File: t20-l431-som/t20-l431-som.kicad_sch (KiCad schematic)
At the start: 2 parts, among them U1 STM32L431-WLCSP64, U2 T20W80

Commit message: Continued initial work on t20-l431 som
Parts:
- removed unit 2 of U2
- removed unit 5 of U2
- removed unit 4 of U2
- U1: footprint (none) -> azonenberg_pcb:BGA_64_0.35MM_3p1MM_STM32L431
- U2: footprint (none) -> azonenberg_pcb:BGA_80_0.4MM_4p4x3p5_T20W80
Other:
- added sheet FPGA config (fpga-config.kicad_sch)
- added sheet Unused banks (unused.kicad_sch)
- sheet Power ports: added 1V8, 3V3, GND, VBAT; removed none
- note added: "Required boot mode straps for SPI x1 mode: * TEST_N high * SS_N high * CBUS[2:0] = 3'b111 We want to avoid needing five external resistors Can we reuse these signals for MCU - FPGA traffic where possible?"
- note added: "TODO: host connection"
- moved on the sheet: U1A, U1B, U1C, U1D, U1E, U2C, U2F, U2G

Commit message: Continued initial layout
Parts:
- added U4: MODULE_INTERNAL_T20_L431_HOST, azonenberg_pcb:MODULE_INTERNAL_T20_L431_HOST, symbol special-azonenberg:MODULE_INTERNAL_T20_L431_HOST
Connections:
- net GPIOL_74_PLLIN0: now reaches U2.A2 (GPIOL_74_PLLIN0)
- net GPIOL_74_PLLIN0: now also U4.B1 (GPIOL_74_PLLIN0)
- net GPIOL_72: now reaches U2.B2 (GPIOL_72_EXTFB0_CDI14)
- net GPIOL_72: now also U4.B2 (GPIOL_72_EXTFB0_CDI14)
- net GPIOL_69_CBSEL1: now reaches U2.C1 (GPIOL_69_CBSEL1)
- net GPIOL_69_CBSEL1: now also U4.B4 (GPIOL_69_CBSEL1)
- net GPIOL_70_CBSEL0: now reaches U2.D1 (GPIOL_70_CBSEL0)
- net GPIOL_70_CBSEL0: now also U4.A4 (GPIOL_70_CBSEL0)
- net GPIOL_71_NSTATUS: now reaches U2.E1 (GPIOL_71_NSTATUS)
- net GPIOL_71_NSTATUS: now also U4.B5 (GPIOL_71_NSTATUS)
- net GPIOL_46: now reaches U2.E2 (GPIOL_46)
- net GPIOL_46: now also U4.C5 (GPIOL_46)
- net GPIOL_25_CLK1: now reaches U2.F1 (GPIOL_25_CLK1)
- net GPIOL_25_CLK1: now also U4.A5 (GPIOL_25_CLK1)
- net GPIOL_24_CLK0: now reaches U2.G1 (GPIOL_24_CLK0)
- net GPIOL_24_CLK0: now also U4.A6 (GPIOL_24_CLK0)
- net GPIOL_20_CTRL0_CDI4: now reaches U2.G2 (GPIOL_20_CTRL0_CDI4)
- net GPIOL_20_CTRL0_CDI4: now also U4.B6 (GPIOL_20_CTRL0_CDI4)
- net GPIOL_13_CDI3: now reaches U2.H1 (GPIOL_13_CDI3)
- net GPIOL_13_CDI3: now also U4.A8 (GPIOL_13_CDI3)
- net GPIOL_12_CDI2: now reaches U2.H2 (GPIOL_12_CDI2)
- net GPIOL_12_CDI2: now also U4.A7 (GPIOL_12_CDI2)
- net GPIOR_133_CDI18: now reaches U2.H7 (GPIOR_133_CDI18)
- net GPIOR_133_CDI18: now also U4.F7 (GPIOR_133_CDI18)
- net CROSS_SPI_MOSI: now reaches U2.H8 (GPIOR_149_CBUS2)
- net CROSS_SPI_MOSI: now also U1.F2 (PB15)
- net GPIOR_154: now reaches U2.J6 (GPIOR_154)
- net GPIOR_154: now also U4.E8 (GPIOR_154)
- net CROSS_SPI_CS_N: now reaches U2.J7 (GPIOR_151_CBUS0)
- net CROSS_SPI_CS_N: now also U1.G3 (PB12)
- net CROSS_SPI_SCK: now reaches U2.J8 (GPIOR_150_CBUS1)
- net CROSS_SPI_SCK: now also U1.G2 (PB13)
- net GPIOR_155: now reaches U2.K6 (GPIOR_155)
- net GPIOR_155: now also U4.E9 (GPIOR_155)
- net CROSS_SPI_MISO: now reaches U2.K7 (GPIOR_158_TEST_N)
- net CROSS_SPI_MISO: now also U1.G1 (PB14)
- net GPIOR_76_PLLIN0: now reaches U2.E7 (GPIOR_76_PLLIN0)
- net GPIOR_76_PLLIN0: now also U4.E5 (GPIOR_76_PLLIN0)
- net GPIOR_116_CTRL15: now reaches U2.G7 (GPIOR_116_CTRL15)
- net GPIOR_116_CTRL15: now also U4.E6 (GPIOR_116_CTRL15)
- net GPIOR_117_CTRL14: now reaches U2.H5 (GPIOR_117_CTRL14)
- net GPIOR_117_CTRL14: now also U4.E7 (GPIOR_117_CTRL14)
- net GPIOR_122_CLK13_CDI21: now reaches U2.H6 (GPIOR_122_CLK13_CDI21)
- net GPIOR_122_CLK13_CDI21: now also U4.F6 (GPIOR_122_CLK13_CDI21)
- net GPIOR_123_CLK12_CDI20: now reaches U2.J5 (GPIOR_123_CLK12_CDI20)
- net GPIOR_123_CLK12_CDI20: now also U4.D8 (GPIOR_123_CLK12_CDI20)
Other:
- sheet Power ports: added 1V8_EN, 2V5_EN, 3V3_FPGA_EN; removed none
- note removed: "TODO: host connection"
- moved on the sheet: U2G

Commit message: Continued initial layout
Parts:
- removed unit 3 of U2
- removed unit 6 of U2
- removed unit 4 of U4
- removed unit 3 of U4
- added C24: 1 uF, azonenberg_pcb:EIA_0201_CAP_NOSILK, symbol device:C
- added unit 8 of U4
- added unit 9 of U4
- added unit 10 of U4
- added unit 7 of U4
- added unit 6 of U4
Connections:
- net GND: now also C24.2
- net MCU_TDI: now reaches U1.A2 (PA15)
- net MCU_TCK: now reaches U1.B2 (PA14)
- net MCU_TCK: now also U4.N6 (MCU_TCK)
- net MCU_TMS: now reaches U1.C2 (PA13)
- net PA4: now reaches U1.E5 (PA4)
- net PA4: now also U4.H4 (PA4)
- net PA5: now reaches U1.F5 (PA5)
- net PA5: now also U4.H3 (PA5)
- net PA2: now reaches U1.F6 (PA2)
- net PA2: now also U4.K1 (PA2)
- net PA0: now reaches U1.F7 (PA0)
- net PA0: now also U4.J1 (PA0)
- net PA6: now reaches U1.G5 (PA6)
- net PA6: now also U4.H5 (PA6)
- net PA3: now reaches U1.G6 (PA3)
- net PA3: now also U4.H1 (PA3)
- net PA1: now reaches U1.G7 (PA1)
- net PA1: now also U4.K3 (PA1)
- net PA7: now reaches U1.H6 (PA7)
- net PA7: now also U4.J2 (PA7)
- net GPIOR_132_CDI19: now reaches U2.G8 (GPIOR_132_CDI19)
- net GPIOR_132_CDI19: now also U4.G7 (GPIOR_132_CDI19)
- net MCU_TDO: now reaches U1.A5 (PB3)
- net PB9: now reaches U1.B6 (PB9)
- net PB9: now also U4.N4 (PB9)
- net PB0: now reaches U1.F4 (PB0)
- net PB0: now also U4.H6 (PB0)
- net PB2: now reaches U1.G4 (PB2)
- net PB2: now also U4.J5 (PB2)
- net PB11: now reaches U1.H3 (PB11)
- net PB11: now also U4.G6 (PB11)
- net PB10: now reaches U1.H4 (PB10)
- net PB10: now also U4.G3 (PB10)
- net PB1: now reaches U1.H5 (PB1)
- net PB1: now also U4.H2 (PB1)
- net PC2: now reaches U1.E7 (PC2)
- net PC2: now also U4.L1 (PC2)
- net PC1: now reaches U1.E8 (PC1)
- net PC1: now also U4.G2 (PC1)
- net PC8: now reaches U1.F3 (PC8)
- net PC8: now also U4.H7 (PC8)
- net MCU_BOOT0: now reaches U1.C5 (BOOT0)
- net MCU_RST_N: now reaches U1.D6 (NRST)
- net MCU_RST_N: now also C24.1
- net PH0: now reaches U1.D8 (PH0)
- net PH0: now also U4.G1 (PH0)
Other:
- added sheet FPGA IO (fpga-io.kicad_sch)
- sheet Power ports: added none; removed VBAT
- moved on the sheet: U2G

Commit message: Continued STM32 fanout
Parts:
- added R4: 10K, azonenberg_pcb:EIA_0201_RES_NOSILK, symbol device:R
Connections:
- net GND: now also R4.2
- net MCU_BOOT0: now also U4.R3 (MCU_BOOT0), R4.1
- net MCU_RST_N: now also U4.L1 (MCU_RST_N)
- net MCU_TDO: now also U4.R2 (MCU_TDO)
- net PA2: now also U4.K2 (PA2); no longer U4.K1 (PA2)
- net PC2: now also U4.K1 (PC2); no longer U4.L1 (PC2)
- net PB7: now reaches U1.A6 (PB7)
- net PB7: now also U4.R1 (PB7)
- net PC13: now reaches U1.B8 (PC13)
- net PC13: now also U4.P1 (PC13)
- net PC15: now reaches U1.C7 (PC15)
- net PC15: now also U4.P2 (PC15)
- net PC14: now reaches U1.C8 (PC14)
- net PC14: now also U4.N1 (PC14)
- net PC0: now reaches U1.D5 (PC0)
- net PC0: now also U4.N2 (PC0)
- net PC3: now reaches U1.E6 (PC3)
- net PC3: now also U4.M2 (PC3)

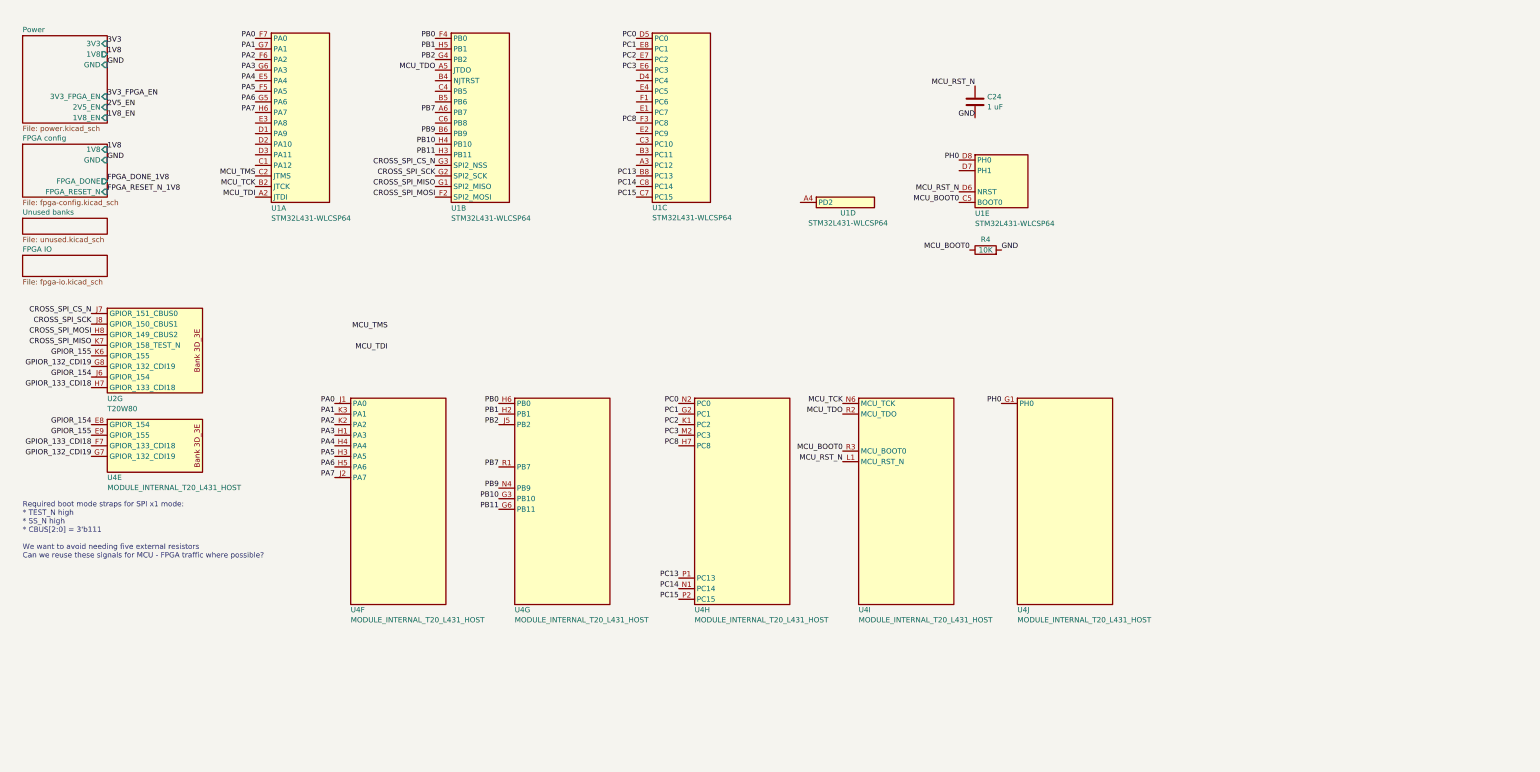
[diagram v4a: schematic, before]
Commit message: Added oscillator
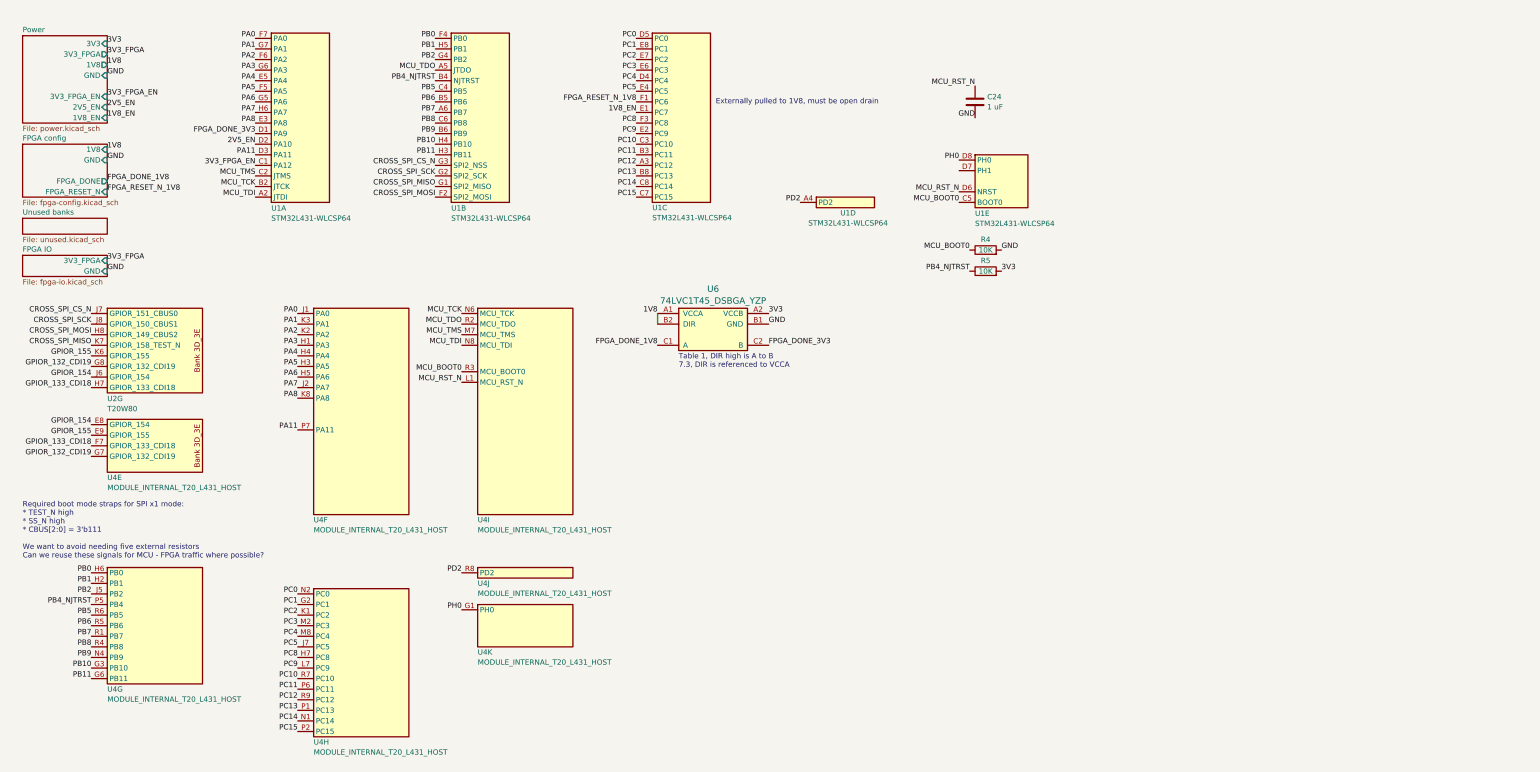
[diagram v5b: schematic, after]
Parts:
- added R5: 10K, azonenberg_pcb:EIA_0201_RES_NOSILK, symbol device:R
- added unit 11 of U4
- added U6: 74LVC1T45_DSBGA_YZP, azonenberg_pcb:BGA_6_1.5x0.9_0.5MM_TI_YZP, symbol special-azonenberg:74LVC1T45_DSBGA_YZP
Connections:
- net 1V8: now also U6.A1 (VCCA), U6.B2 (DIR)
- net 1V8_EN: now also U1.E1 (PC7)
- net 2V5_EN: now also U1.D2 (PA10)
- net 3V3: now also R5.2, U6.A2 (VCCB)
- net 3V3_FPGA_EN: now also U1.C1 (PA12)
- net FPGA_DONE_1V8: now also U6.C1 (A)
- net FPGA_RESET_N_1V8: now also U1.F1 (PC6)
- net GND: now also U6.B1 (GND)
- net MCU_TDI: now also U4.N8 (MCU_TDI)
- net MCU_TMS: now also U4.M7 (MCU_TMS)
- net PH0: now also U4.G1 (PH0); no longer U4.G1 (PH0)
- net FPGA_DONE_3V3: now reaches U1.D1 (PA9)
- net FPGA_DONE_3V3: now also U6.C2 (B)
- net PA11: now reaches U1.D3 (PA11)
- net PA11: now also U4.P7 (PA11)
- net PA8: now reaches U1.E3 (PA8)
- net PA8: now also U4.K8 (PA8)
- net PB4_NJTRST: now reaches U1.B4 (PB4)
- net PB4_NJTRST: now also U4.P5 (PB4), R5.1
- net PB6: now reaches U1.B5 (PB6)
- net PB6: now also U4.R5 (PB6)
- net PB5: now reaches U1.C4 (PB5)
- net PB5: now also U4.R6 (PB5)
- net PB8: now reaches U1.C6 (PB8)
- net PB8: now also U4.R4 (PB8)
- net PC12: now reaches U1.A3 (PC12)
- net PC12: now also U4.R9 (PC12)
- net PC11: now reaches U1.B3 (PC11)
- net PC11: now also U4.P6 (PC11)
- net PC10: now reaches U1.C3 (PC10)
- net PC10: now also U4.R7 (PC10)
- net PC4: now reaches U1.D4 (PC4)
- net PC4: now also U4.M8 (PC4)
- net PC9: now reaches U1.E2 (PC9)
- net PC9: now also U4.L7 (PC9)
- net PC5: now reaches U1.E4 (PC5)
- net PC5: now also U4.J7 (PC5)
- net PD2: now reaches U1.A4 (PD2)
- net PD2: now also U4.R8 (PD2)
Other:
- sheet FPGA IO ports: added 3V3_FPGA, GND; removed none
- sheet Power ports: added 3V3_FPGA; removed none
- note added: "Externally pulled to 1V8, must be open drain"
- note added: "Table 1, DIR high is A to B 7.3, DIR is referenced to VCCA"
- moved on the sheet: U4J

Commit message: Finished initial L431 SOM routing
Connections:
- net PC0: now also U4.~ (PC0); no longer U4.N2 (PC0)
- net PH1: now reaches U1.D7 (PH1)
- net PH1: now also U4.N2 (PH1)
- net PA11 renamed 1V2_EN
- net 1V2_EN: no longer U4.P7 (PA11)
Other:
- sheet Power ports: added 1V2_EN; removed none
- moved on the sheet: U1D, U4I, U4J, U6

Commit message: Continued L431 SoM layout
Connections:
- net MCU_BOOT0: now also U4.R6 (MCU_BOOT0); no longer U4.R3 (MCU_BOOT0)
- net MCU_TCK: now also U4.P7 (MCU_TCK); no longer U4.N6 (MCU_TCK)
- net MCU_TDO: now also U4.R3 (MCU_TDO); no longer U4.R2 (MCU_TDO)
- net MCU_TMS: now also U4.L9 (MCU_TMS); no longer U4.M7 (MCU_TMS)
- net PB5: now also U4.R7 (PB5); no longer U4.R6 (PB5)
- net PB7: now also U4.R2 (PB7); no longer U4.R1 (PB7)
- net PC0: now also U4.P2 (PC0); no longer U4.~ (PC0)
- net PC10: now also U4.P6 (PC10); no longer U4.R7 (PC10)
- net PC11: now also U4.N6 (PC11); no longer U4.P6 (PC11)
- net PC15: now also U4.R1 (PC15); no longer U4.P2 (PC15)

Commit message: More work on T20-L431 module
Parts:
- added C33: 1 uF, azonenberg_pcb:EIA_0201_CAP_NOSILK, symbol device:C
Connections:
- net 3V3: now also C33.1
- net GND: now also C33.2
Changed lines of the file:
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@@
 		)
 	)
+	(label "3V3"
+		(at 210.82 80.01 0)
+		(effects
+			(font
+				(size 1.27 1.27)
+			)
+			(justify left bottom)
+		)
+	)
 	(label "GND"
 		(at 35.56 74.93 0)
@@
 		)
 	)
+	(label "GND"
+		(at 210.82 87.63 0)
+		(effects
+			(font
+				(size 1.27 1.27)
+			)
+			(justify left bottom)
+		)
+	)
 	(label "PD2"
 		(at 133.35 168.91 180)
@@
 		(pin "P7"
 		)
+		(pin "L11"
+		)
+		(pin "K10"
+		)
+		(pin "R11"
+		)
+		(pin "N11"
+		)
+		(pin "L10"
+		)
+		(pin "R10"
+		)
 		(instances
 			(project "t20-l431-som"
@@
 	(symbol
 		(lib_id "device:C")
+		(at 210.82 83.82 0)
+		(unit 1)
+		(exclude_from_sim no)
+		(in_bom yes)
+		(on_board yes)
+		(dnp no)
+		(fields_autoplaced yes)
+		(property "Reference" "C33"
+			(at 213.741 82.6078 0)
+			(effects
+				(font
+					(size 1.27 1.27)
+				)
+				(justify left)
+			)
+		)
+		(property "Value" "1 uF"
+			(at 213.741 85.0321 0)
+			(effects
+				(font
+					(size 1.27 1.27)
+				)
+				(justify left)
+			)
+		)
+		(property "Footprint" "azonenberg_pcb:EIA_0201_CAP_NOSILK"
+			(at 211.7852 87.63 0)
+			(effects
+				(font
+					(size 1.27 1.27)
+				)
+				(hide yes)
+			)
+		)
+		(property "Datasheet" ""
+			(at 210.82 83.82 0)
+			(effects
+				(font
+					(size 1.27 1.27)
+				)
+				(hide yes)
+			)
+		)
+		(property "Description" "Unpolarized capacitor"
+			(at 210.82 83.82 0)
+			(effects
+				(font
+					(size 1.27 1.27)
+				)
+				(hide yes)
+			)
+		)
+		(property "MPN" "GRM033C80J105ME05D"
+			(at 210.82 83.82 0)
+			(effects
+				(font
+					(size 1.27 1.27)
+				)
+				(hide yes)
+			)
+		)
+		(pin "2"
+		)
+		(pin "1"
+		)
+		(instances
+			(project "t20-l431-som"
+				(path "/c9028163-a5a7-4e78-bba9-fb79df7846cd"
+					(reference "C33")
+					(unit 1)
+				)
+			)
+		)
+	)
+	(symbol
+		(lib_id "device:C")
 		(at 243.84 34.29 0)
 		(unit 1)
@@
 		(pin "P7"
 		)
+		(pin "L11"
+		)
+		(pin "R11"
+		)
+		(pin "K10"
+		)
+		(pin "N11"
+		)
+		(pin "L10"
+		)
+		(pin "R10"
+		)
 		(instances
 			(project "t20-l431-som"
@@
 		(pin "P10"
 		)
+		(pin "L11"
+		)
+		(pin "K10"
+		)
+		(pin "R11"
+		)
+		(pin "N11"
+		)
+		(pin "L10"
+		)
+		(pin "R10"
+		)
 		(instances
 			(project "t20-l431-som"
@@
 		(pin "P7"
 		)
+		(pin "L11"
+		)
+		(pin "K10"
+		)
+		(pin "R11"
+		)
+		(pin "N11"
+		)
+		(pin "L10"
+		)
+		(pin "R10"
+		)
 		(instances
 			(project "t20-l431-som"
@@
 		(pin "P7"
 		)
+		(pin "K10"
+		)
+		(pin "R11"
+		)
+		(pin "N11"
+		)
+		(pin "L11"
+		)
+		(pin "L10"
+		)
+		(pin "R10"
+		)
 		(instances
 			(project "t20-l431-som"
@@
 		(pin "M10"
 		)
+		(pin "N11"
+		)
+		(pin "L10"
+		)
+		(pin "R10"
+		)
+		(pin "L11"
+		)
+		(pin "K10"
+		)
+		(pin "R11"
+		)
 		(instances
 			(project "t20-l431-som"
@@
 		(pin "M10"
 		)
+		(pin "K10"
+		)
+		(pin "R11"
+		)
+		(pin "N11"
+		)
+		(pin "L10"
+		)
+		(pin "R10"
+		)
+		(pin "L11"
+		)
 		(instances
